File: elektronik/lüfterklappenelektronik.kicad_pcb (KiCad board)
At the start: 4 copper layers, 80 x 87.6 mm, 115 parts, among them J101 Conn_01x05_Male, J102 Ckmtw_2510S-2P, J103 Conn_LAN_ENC28J60, J104 USB_B_Micro, J106 WJ2EDGRC-5.08-2P, J107 WJ2EDGRC-5.08-2P, J108 WJ2EDGRC-5.08-2P, P101 PWR_BUS_CONN1, P103 PressureSensor3, P104 PressureSensor1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

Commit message: placing mostly done
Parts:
- moved C117 1.27 mm to (87.6, 96.5)
- moved C119 1.27 mm to (81.3, 96.5)
- moved L102 1.27 mm to (90.2, 96.5)
- moved L105 1.27 mm to (85.1, 96.5)
- moved C126 1.27 mm to (86.4, 86.4)
- moved D102 1.27 mm to (97.8, 99.1)
- moved D107 1.27 mm to (85.1, 100.3)
- moved J107 1.27 mm to (95.2, 91.4)
- moved Q102 1.27 mm to (96.5, 106.7)
- moved R102 1.27 mm to (90.2, 100.3)
- moved R105 1.27 mm to (81.3, 100.3)
- moved R110 1.27 mm to (87.6, 104.1)
- moved R132 1.27 mm to (82.5, 104.1)
- moved U102 1.27 mm to (90.2, 91.4)
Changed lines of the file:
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@@
   )
   (module FootprintsTittelbach:WJ2EDGRC-5.08-2P (layer F.Cu)
-    (at 95.25 92.71)
+    (at 95.25 91.44)
     (descr "terminal block RND 205-00289, 4 pins, pitch 5.08mm, size 20.3x10.6mm^2, drill diamater 1.3mm, pad diameter 2.5mm, see http://cdn-reichelt.de/documents/datenblatt/C151/RND_205-00287_DB_EN.pdf, script-generated using https://github.com/pointhi/kicad-footprint-generator/scripts/TerminalBlock_RND")
     (tags "THT terminal block RND 205-00289 pitch 5.08mm size 20.3x10.6mm^2 drill 1.3mm pad 2.5mm")
@@
   )
   (module Resistor_SMD:R_0603_1608Metric (layer F.Cu)
-    (at 87.63 105.41 270)
+    (at 87.63 104.14 270)
     (descr "Resistor SMD 0603 (1608 Metric), square (rectangular) end terminal, IPC_7351 nominal, (Body size source: http://www.tortai-tech.com/upload/download/2011102023233369053.pdf), generated with kicad-footprint-generator")
     (tags resistor)
@@
   )
   (module Resistor_SMD:R_0603_1608Metric (layer F.Cu)
-    (at 81.28 101.6 270)
+    (at 81.28 100.33 270)
     (descr "Resistor SMD 0603 (1608 Metric), square (rectangular) end terminal, IPC_7351 nominal, (Body size source: http://www.tortai-tech.com/upload/download/2011102023233369053.pdf), generated with kicad-footprint-generator")
     (tags resistor)
@@
   )
   (module Resistor_SMD:R_0603_1608Metric (layer F.Cu)
-    (at 90.17 101.6 90)
+    (at 90.17 100.33 90)
     (descr "Resistor SMD 0603 (1608 Metric), square (rectangular) end terminal, IPC_7351 nominal, (Body size source: http://www.tortai-tech.com/upload/download/2011102023233369053.pdf), generated with kicad-footprint-generator")
     (tags resistor)
@@
   )
   (module Diode_SMD:D_SOD-323 (layer F.Cu)
-    (at 85.09 101.6 270)
+    (at 85.09 100.33 270)
     (descr SOD-323)
     (tags SOD-323)
@@
   )
   (module Package_TO_SOT_SMD:TO-252-2 (layer F.Cu)
-    (at 96.52 107.95)
+    (at 96.52 106.68)
     (descr "TO-252 / DPAK SMD package, http://www.infineon.com/cms/en/product/packages/PG-TO252/PG-TO252-3-1/")
     (tags "DPAK TO-252 DPAK-3 TO-252-3 SOT-428")
@@
   )
   (module FootprintsTittelbach:Ckmtw_2510S-4P (layer F.Cu)
-    (at 90.17 92.71 180)
+    (at 90.17 91.44 180)
     (fp_text reference U102 (at 3.75 1.75) (layer F.SilkS)
       (effects (font (size 1 1) (thickness 0.15)))
@@
   )
   (module Diode_SMD:D_SMB (layer F.Cu)
-    (at 97.79 100.33)
+    (at 97.79 99.06)
     (descr "Diode SMB (DO-214AA)")
     (tags "Diode SMB (DO-214AA)")
@@
   )
   (module Capacitor_SMD:C_0603_1608Metric (layer F.Cu)
-    (at 87.63 97.79 90)
+    (at 87.63 96.52 90)
     (descr "Capacitor SMD 0603 (1608 Metric), square (rectangular) end terminal, IPC_7351 nominal, (Body size source: http://www.tortai-tech.com/upload/download/2011102023233369053.pdf), generated with kicad-footprint-generator")
     (tags capacitor)
@@
   )
   (module Capacitor_SMD:C_0603_1608Metric (layer F.Cu)
-    (at 81.28 97.79 90)
+    (at 81.28 96.52 90)
     (descr "Capacitor SMD 0603 (1608 Metric), square (rectangular) end terminal, IPC_7351 nominal, (Body size source: http://www.tortai-tech.com/upload/download/2011102023233369053.pdf), generated with kicad-footprint-generator")
     (tags capacitor)
@@
   )
   (module Inductor_SMD:L_0603_1608Metric_Pad1.05x0.95mm_HandSolder (layer F.Cu)
-    (at 90.17 97.79 270)
+    (at 90.17 96.52 270)
     (descr "Capacitor SMD 0603 (1608 Metric), square (rectangular) end terminal, IPC_7351 nominal with elongated pad for handsoldering. (Body size source: http://www.tortai-tech.com/upload/download/2011102023233369053.pdf), generated with kicad-footprint-generator")
     (tags "inductor handsolder")
@@
   )
   (module Inductor_SMD:L_0603_1608Metric_Pad1.05x0.95mm_HandSolder (layer F.Cu)
-    (at 85.09 97.79 90)
+    (at 85.09 96.52 90)
     (descr "Capacitor SMD 0603 (1608 Metric), square (rectangular) end terminal, IPC_7351 nominal with elongated pad for handsoldering. (Body size source: http://www.tortai-tech.com/upload/download/2011102023233369053.pdf), generated with kicad-footprint-generator")
     (tags "inductor handsolder")
@@
   )
   (module Resistor_SMD:R_0603_1608Metric (layer F.Cu)
-    (at 82.55 105.41 180)
+    (at 82.55 104.14 180)
     (descr "Resistor SMD 0603 (1608 Metric), square (rectangular) end terminal, IPC_7351 nominal, (Body size source: http://www.tortai-tech.com/upload/download/2011102023233369053.pdf), generated with kicad-footprint-generator")
     (tags resistor)
@@
   )
   (module Capacitor_SMD:C_0603_1608Metric (layer F.Cu)
-    (at 86.36 87.63)
+    (at 86.36 86.36)
     (descr "Capacitor SMD 0603 (1608 Metric), square (rectangular) end terminal, IPC_7351 nominal, (Body size source: http://www.tortai-tech.com/upload/download/2011102023233369053.pdf), generated with kicad-footprint-generator")
     (tags capacitor)
@@
     (effects (font (size 1.5 1.5) (thickness 0.3)))
   )
-  (gr_text "Damper2\nMotor" (at 97.79 86.36 180) (layer F.SilkS)
+  (gr_text "Damper2\nMotor" (at 97.79 85.09 180) (layer F.SilkS)
     (effects (font (size 1.5 1.5) (thickness 0.3)))
   )
@@
     (effects (font (size 1.5 1.5) (thickness 0.3)) (justify right))
   )
-  (gr_text "D2\nEndstop" (at 81.28 86.36 180) (layer F.SilkS)
+  (gr_text "D2\nEndstop" (at 81.28 85.09 180) (layer F.SilkS)
     (effects (font (size 1.5 1.5) (thickness 0.3)) (justify right))
   )

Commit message: placing improved
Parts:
- moved C106 113.1 mm to (66.0, 81.3), turned to 180 degrees
- moved C103 111.9 mm to (66.0, 86.4), turned to 180 degrees
- moved C105 103.4 mm to (94.0, 73.7)
- moved C107 65.5 mm to (92.7, 52.1), turned to 90 degrees
- moved C104 61.9 mm to (86.4, 52.1), turned to 90 degrees
- moved R134 22.2 mm to (72.4, 80.0), turned to 180 degrees
- moved D109 21.3 mm to (73.7, 83.8), turned to 180 degrees
- moved C115 18.3 mm to (64.8, 61.0), turned to 90 degrees
- moved Q105 17.6 mm to (77.5, 64.8), turned to 270 degrees
- moved R128 16.6 mm to (64.8, 66.0)
- moved R131 16.6 mm to (66.0, 73.7)
- moved R127 16.5 mm to (64.8, 69.8)
- moved R116 16.3 mm to (81.3, 64.8), turned to 270 degrees
- moved R118 15.5 mm to (77.5, 81.3)
- moved L111 15.3 mm to (78.7, 86.4)
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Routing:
- net /UCD+: track 2.58 -> 7.15 mm
- net /UCD-: track 2.58 -> 7.06 mm
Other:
- net class 12V added: clearance 0.2, trace_width 0.8, via_dia 0.6, via_drill 0.4
- net class 3V3 added: clearance 0.2, trace_width 0.4, via_dia 0.6, via_drill 0.4
- net class 5V added: clearance 0.2, trace_width 0.5, via_dia 0.6, via_drill 0.4
- net class Default: trace_width 0.4 -> 0.3

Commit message: basic routing, drc passed
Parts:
- moved D115 45.3 mm to (72.4, 99.1), turned to 90 degrees
- moved R123 35.0 mm to (100.3, 73.7), turned to 90 degrees
- moved R112 16.0 mm to (103.5, 73.0)
- moved R126 15.7 mm to (64.8, 55.9), turned to 90 degrees
- moved D117 14.5 mm to (137.2, 68.6), turned to 0 degrees
- moved C109 14.3 mm to (117.0, 71.8), turned to 0 degrees
- moved D105 11.5 mm to (106.7, 72.4), turned to 180 degrees
- moved C125 11.4 mm to (95.1, 133.3), turned to 180 degrees
- moved C121 11.4 mm to (100.3, 123.2), turned to 270 degrees
- moved R127 10.2 mm to (64.8, 59.7)
- moved R119 9.37 mm to (113.0, 87.6)
- moved C115 7.62 mm to (64.8, 68.6), turned to 270 degrees
- moved D112 5.68 mm to (114.3, 90.2), turned to 0 degrees
- moved D110 5.08 mm to (134.6, 90.2)
- moved R121 5.08 mm to (132.1, 90.2)
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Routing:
- net GND: track 0.00 -> 567.5 mm, vias 0 -> 17
- net +3V3: track 0.00 -> 313.5 mm, vias 0 -> 17
- net +12V: track 0.00 -> 159.6 mm
- net /PJON: track 0.00 -> 118.2 mm
- net +5V: track 0.00 -> 107.3 mm
- net /Damper2: track 0.00 -> 99.6 mm, vias 0 -> 2
- net /EndstopDamper2: track 0.00 -> 91.1 mm, vias 0 -> 4
- net /IO0: track 0.00 -> 88.7 mm, vias 0 -> 2
- net /Damper3: track 0.00 -> 87.0 mm, vias 0 -> 2
- net /Damper1: track 0.00 -> 81.0 mm, vias 0 -> 2
- net /EndstopDamper1: track 0.00 -> 76.4 mm, vias 0 -> 2
- net /VBUS: track 0.00 -> 71.3 mm, vias 0 -> 2
- net /EndstopDamper3: track 0.00 -> 70.8 mm, vias 0 -> 2
- net /MOSI: track 0.00 -> 69.1 mm
- net /RXD: track 0.00 -> 55.5 mm, vias 0 -> 2
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- added copper zone on F.Cu, net +3V3
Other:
- net class 12V: clearance 0.2 -> 0.25
- net class 3V3: clearance 0.2 -> 0.25
- net class 5V: clearance 0.2 -> 0.25
- net class Default: clearance 0.2 -> 0.25
- rule trace_clearance: 0.2 -> 0.25
- board text added: "3V3 GND SCK Mosi CS Miso"
- board text removed: "3V3 GND SCK MOSI CS MISO"

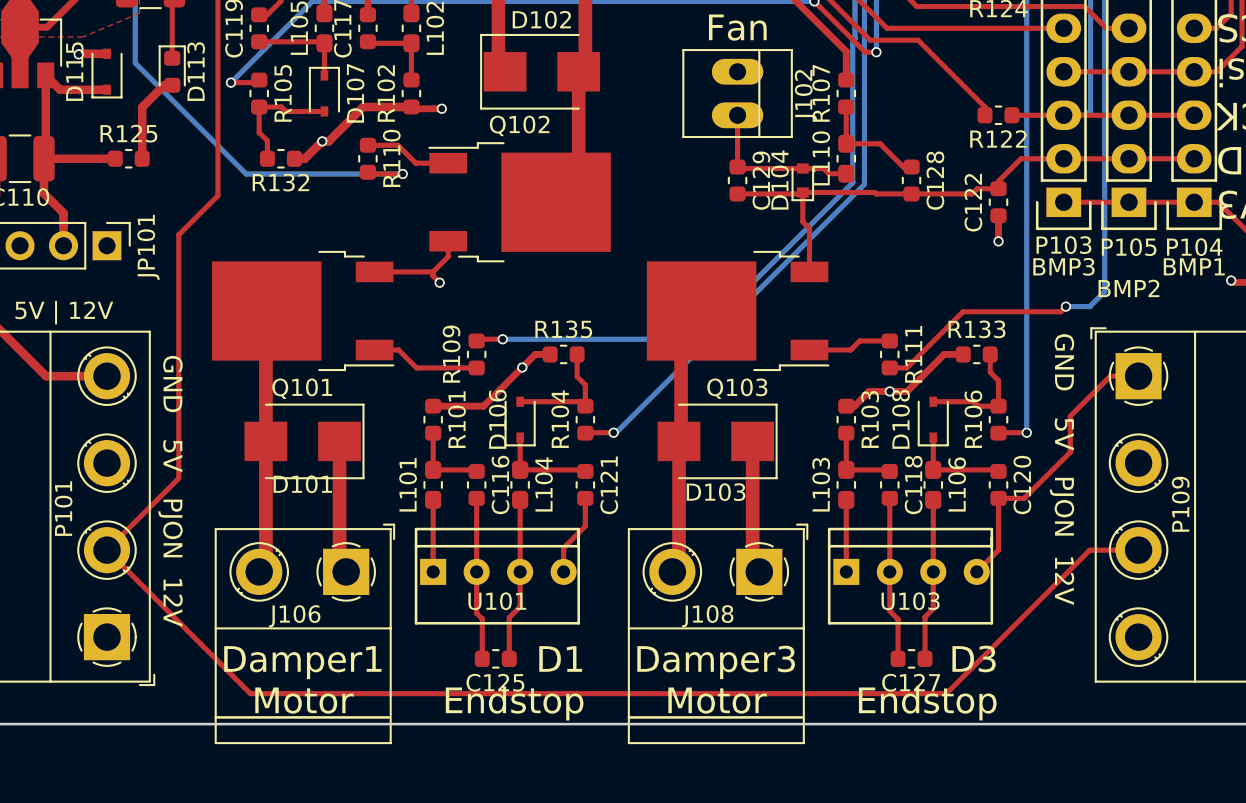
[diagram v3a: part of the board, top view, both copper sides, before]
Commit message: power routing, drc passed
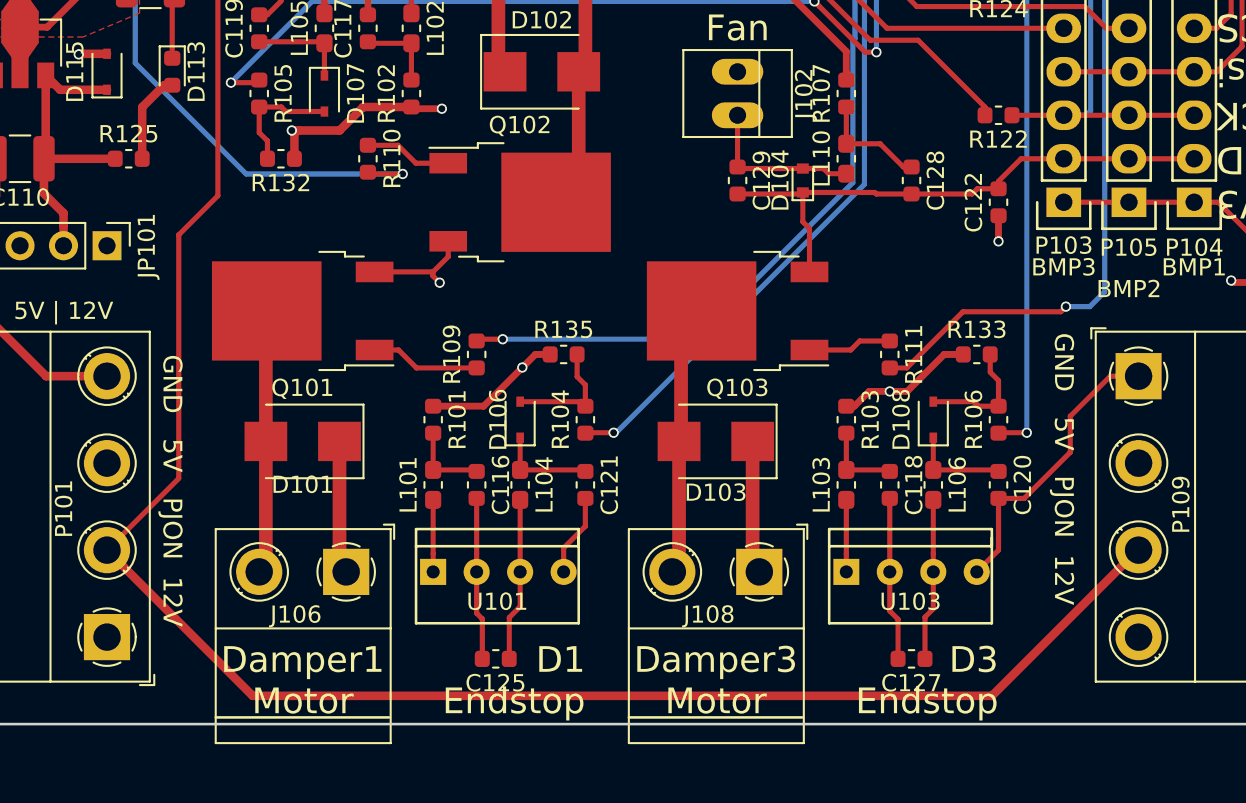
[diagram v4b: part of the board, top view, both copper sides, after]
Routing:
- net +5V: track 107.3 -> 110.1 mm
- net +3V3: track 313.5 -> 312.7 mm
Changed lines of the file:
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@@
     (thickness 1.6)
     (drawings 34)
-    (tracks 949)
+    (tracks 950)
     (zones 0)
     (modules 115)
@@
   (segment (start 95.25 98.67) (end 95.64 99.06) (width 0.8) (layer F.Cu) (net 1))
   (segment (start 95.25 91.44) (end 95.25 98.67) (width 0.8) (layer F.Cu) (net 1))
-  (segment (start 72.39 129.93) (end 72.39 132.08) (width 0.8) (layer In2.Cu) (net 1))
-  (segment (start 74.390001 127.929999) (end 72.39 129.93) (width 0.8) (layer In2.Cu) (net 1))
-  (segment (start 74.390001 109.570001) (end 74.390001 127.929999) (width 0.8) (layer In2.Cu) (net 1))
-  (segment (start 74.04 109.22) (end 74.390001 109.570001) (width 0.8) (layer In2.Cu) (net 1))
-  (segment (start 72.39 109.22) (end 74.04 109.22) (width 0.8) (layer In2.Cu) (net 1))
-  (segment (start 86.36 130.42) (end 86.36 128.27) (width 0.8) (layer In2.Cu) (net 1))
-  (segment (start 84.7 132.08) (end 86.36 130.42) (width 0.8) (layer In2.Cu) (net 1))
-  (segment (start 72.39 132.08) (end 84.7 132.08) (width 0.8) (layer In2.Cu) (net 1))
-  (segment (start 84.7 132.08) (end 109.347 132.08) (width 0.8) (layer In2.Cu) (net 1))
-  (segment (start 110.49 130.937) (end 110.49 128.27) (width 0.8) (layer In2.Cu) (net 1))
-  (segment (start 109.347 132.08) (end 110.49 130.937) (width 0.8) (layer In2.Cu) (net 1))
-  (segment (start 86.36 98.18) (end 93.1 91.44) (width 0.8) (layer In2.Cu) (net 1))
-  (segment (start 93.1 91.44) (end 95.25 91.44) (width 0.8) (layer In2.Cu) (net 1))
-  (segment (start 86.36 128.27) (end 86.36 98.18) (width 0.8) (layer In2.Cu) (net 1))
-  (segment (start 132.64 132.08) (end 109.347 132.08) (width 0.8) (layer In2.Cu) (net 1))
+  (segment (start 86.36 130.42) (end 86.36 128.27) (width 2) (layer In2.Cu) (net 1))
+  (segment (start 84.7 132.08) (end 86.36 130.42) (width 2) (layer In2.Cu) (net 1))
+  (segment (start 72.39 132.08) (end 84.7 132.08) (width 3) (layer In2.Cu) (net 1))
+  (segment (start 84.7 132.08) (end 109.347 132.08) (width 3) (layer In2.Cu) (net 1))
+  (segment (start 110.49 130.937) (end 110.49 128.27) (width 2) (layer In2.Cu) (net 1))
+  (segment (start 109.347 132.08) (end 110.49 130.937) (width 2) (layer In2.Cu) (net 1))
+  (segment (start 132.64 132.08) (end 109.347 132.08) (width 3) (layer In2.Cu) (net 1))
   (segment (start 85.97 127.88) (end 86.36 128.27) (width 0.8) (layer F.Cu) (net 1))
   (segment (start 85.97 120.65) (end 85.97 127.88) (width 0.8) (layer F.Cu) (net 1))
   (segment (start 110.1 127.88) (end 110.49 128.27) (width 0.8) (layer F.Cu) (net 1))
   (segment (start 110.1 120.65) (end 110.1 127.88) (width 0.8) (layer F.Cu) (net 1))
+  (segment (start 72.644 132.08) (end 72.39 132.08) (width 1) (layer In2.Cu) (net 1))
+  (segment (start 72.39 109.22) (end 74.04 109.22) (width 1) (layer In2.Cu) (net 1))
+  (segment (start 74.04 109.22) (end 75.565 110.745) (width 1) (layer In2.Cu) (net 1))
+  (segment (start 75.565 110.745) (end 75.565 129.159) (width 1) (layer In2.Cu) (net 1))
+  (segment (start 75.565 129.159) (end 72.644 132.08) (width 1) (layer In2.Cu) (net 1))
+  (segment (start 95.25 91.948) (end 95.25 91.44) (width 2) (layer In2.Cu) (net 1))
+  (segment (start 86.36 100.838) (end 95.25 91.948) (width 2) (layer In2.Cu) (net 1))
+  (segment (start 86.36 128.27) (end 86.36 100.838) (width 2) (layer In2.Cu) (net 1))
   (segment (start 81.67 127.88) (end 81.28 128.27) (width 0.8) (layer F.Cu) (net 2))
   (segment (start 81.67 120.65) (end 81.67 127.88) (width 0.8) (layer F.Cu) (net 2))
@@
   (segment (start 133.022 114.808) (end 132.64 115.19) (width 0.3) (layer In1.Cu) (net 5))
   (segment (start 134.112 114.808) (end 133.022 114.808) (width 0.3) (layer In1.Cu) (net 5))
-  (segment (start 67.31 116.84) (end 72.39 121.92) (width 0.5) (layer In2.Cu) (net 6))
-  (segment (start 67.31 109.22) (end 67.31 116.84) (width 0.5) (layer In2.Cu) (net 6))
-  (segment (start 70.539999 133.830001) (end 71.710998 135.001) (width 0.5) (layer In2.Cu) (net 6))
-  (segment (start 70.539999 123.770001) (end 70.539999 133.830001) (width 0.5) (layer In2.Cu) (net 6))
-  (segment (start 72.39 121.92) (end 70.539999 123.770001) (width 0.5) (layer In2.Cu) (net 6))
-  (segment (start 132.457002 135.001) (end 137.795 129.663002) (width 0.5) (layer In2.Cu) (net 6))
-  (segment (start 71.710998 135.001) (end 132.457002 135.001) (width 0.5) (layer In2.Cu) (net 6))
-  (segment (start 137.795 127.075) (end 132.64 121.92) (width 0.5) (layer In2.Cu) (net 6))
-  (segment (start 137.795 129.663002) (end 137.795 127.075) (width 0.5) (layer In2.Cu) (net 6))
+  (segment (start 67.31 116.84) (end 72.39 121.92) (width 1) (layer In2.Cu) (net 6))
+  (segment (start 67.31 109.22) (end 67.31 116.84) (width 1) (layer In2.Cu) (net 6))
+  (segment (start 136.525 125.805) (end 132.64 121.92) (width 1.5) (layer In2.Cu) (net 6))
+  (segment (start 72.39 121.92) (end 68.961 125.349) (width 1.5) (layer In2.Cu) (net 6))
+  (segment (start 68.961 125.349) (end 68.961 133.858) (width 1.5) (layer In2.Cu) (net 6))
+  (segment (start 70.485 135.382) (end 134.239 135.382) (width 1.5) (layer In2.Cu) (net 6))
+  (segment (start 134.239 135.382) (end 136.525 133.096) (width 1.5) (layer In2.Cu) (net 6))
+  (segment (start 136.525 133.096) (end 136.525 125.805) (width 1.5) (layer In2.Cu) (net 6))
+  (segment (start 68.961 133.858) (end 70.485 135.382) (width 1.5) (layer In2.Cu) (net 6))
   (segment (start 77.865 83.82) (end 80.01 85.965) (width 0.3) (layer F.Cu) (net 7))
   (segment (start 74.36 83.82) (end 77.865 83.82) (width 0.3) (layer F.Cu) (net 7))
@@
   (segment (start 76.581 122.809) (end 72.39 127) (width 0.3) (layer F.Cu) (net 7))
   (segment (start 76.581 108.585) (end 76.581 122.809) (width 0.3) (layer F.Cu) (net 7))
-  (segment (start 80.772 135.382) (end 72.39 127) (width 0.3) (layer F.Cu) (net 7))
-  (segment (start 121.412 135.382) (end 80.772 135.382) (width 0.3) (layer F.Cu) (net 7))
-  (segment (start 129.794 127) (end 121.412 135.382) (width 0.3) (layer F.Cu) (net 7))
-  (segment (start 132.64 127) (end 129.794 127) (width 0.3) (layer F.Cu) (net 7))
+  (segment (start 80.899 135.509) (end 72.39 127) (width 0.5) (layer F.Cu) (net 7))
+  (segment (start 124.079 135.509) (end 80.899 135.509) (width 0.5) (layer F.Cu) (net 7))
+  (segment (start 132.588 127) (end 124.079 135.509) (width 0.5) (layer F.Cu) (net 7))
+  (segment (start 132.64 127) (end 132.588 127) (width 0.5) (layer F.Cu) (net 7))
   (segment (start 95.51 61.595) (end 92.964 64.141) (width 0.4) (layer F.Cu) (net 8))
   (segment (start 96.91 61.595) (end 95.51 61.595) (width 0.4) (layer F.Cu) (net 8))
@@
   (segment (start 121.285 115.57) (end 122.4025 115.57) (width 0.4) (layer F.Cu) (net 16))
   (segment (start 119.126 117.729) (end 121.285 115.57) (width 0.4) (layer F.Cu) (net 16))
-  (segment (start 83.947 104.14) (end 83.3375 104.14) (width 0.5) (layer F.Cu) (net 16))
-  (via (at 84.963 103.124) (size 0.6) (drill 0.4) (layers F.Cu B.Cu) (net 16))
-  (segment (start 84.963 103.124) (end 83.947 104.14) (width 0.5) (layer F.Cu) (net 16))
   (segment (start 118.11 117.729) (end 119.126 117.729) (width 0.4) (layer F.Cu) (net 16))
   (via (at 118.11 117.729) (size 0.6) (drill 0.4) (layers F.Cu B.Cu) (net 16))
@@
   (segment (start 90.2715 101.219) (end 90.17 101.1175) (width 0.4) (layer F.Cu) (net 16))
   (segment (start 91.948 101.219) (end 90.2715 101.219) (width 0.4) (layer F.Cu) (net 16))
-  (segment (start 85.344 103.124) (end 84.963 103.124) (width 0.5) (layer F.Cu) (net 16))
-  (segment (start 87.3505 101.1175) (end 85.344 103.124) (width 0.5) (layer F.Cu) (net 16))
-  (segment (start 90.17 101.1175) (end 87.3505 101.1175) (width 0.5) (layer F.Cu) (net 16))
   (segment (start 100.33 106.045) (end 96.52 106.045) (width 0.4) (layer In2.Cu) (net 16))
   (segment (start 109.22 99.06) (end 107.315 99.06) (width 0.4) (layer In2.Cu) (net 16))
@@
   (segment (start 123.825 108.966) (end 113.919 99.06) (width 0.4) (layer In2.Cu) (net 16))
   (via (at 71.12 94.234) (size 0.6) (drill 0.4) (layers F.Cu B.Cu) (net 16))
-  (segment (start 80.01 103.124) (end 71.12 94.234) (width 0.4) (layer In2.Cu) (net 16))
-  (segment (start 84.963 103.124) (end 80.01 103.124) (width 0.4) (layer In2.Cu) (net 16))
   (segment (start 73.276 94.234) (end 73.53 93.98) (width 0.4) (layer F.Cu) (net 16))
   (segment (start 71.12 94.234) (end 73.276 94.234) (width 0.4) (layer F.Cu) (net 16))
@@
   (segment (start 124.46 110.109) (end 124.46 111.379) (width 0.4) (layer In2.Cu) (net 16))
   (segment (start 124.46 108.966) (end 124.46 110.109) (width 0.4) (layer In2.Cu) (net 16))
+  (segment (start 79.375 102.489) (end 83.185 102.489) (width 0.4) (layer In2.Cu) (net 16))
+  (segment (start 71.12 94.234) (end 79.375 102.489) (width 0.4) (layer In2.Cu) (net 16))
+  (segment (start 83.609264 102.489) (end 83.185 102.489) (width 0.5) (layer F.Cu) (net 16))
+  (segment (start 85.979 102.489) (end 83.609264 102.489) (width 0.5) (layer F.Cu) (net 16))
+  (segment (start 90.17 101.1175) (end 87.3505 101.1175) (width 0.5) (layer F.Cu) (net 16))
+  (segment (start 83.3375 102.6415) (end 83.185 102.489) (width 0.5) (layer F.Cu) (net 16))
+  (segment (start 83.3375 104.14) (end 83.3375 102.6415) (width 0.5) (layer F.Cu) (net 16))
+  (segment (start 87.3505 101.1175) (end 85.979 102.489) (width 0.5) (layer F.Cu) (net 16))
+  (via (at 83.185 102.489) (size 0.6) (drill 0.4) (layers F.Cu B.Cu) (net 16))
   (segment (start 115.7675 71.755) (end 116.205 71.755) (width 0.3) (layer F.Cu) (net 17))
   (segment (start 113.91 69.8975) (end 115.7675 71.755) (width 0.3) (layer F.Cu) (net 17))
